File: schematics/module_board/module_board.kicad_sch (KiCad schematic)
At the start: 26 parts, among them J1 Conn_01x04_Male, J10 Conn_01x02_Male, J2 Conn_01x10_Male, J5 Conn_01x06_Male, J9 Conn_01x02_Male, U1 RP2040, U2 W25Q16JVSSIQ, Y1 ABLS-12.000MHZ-B4-T

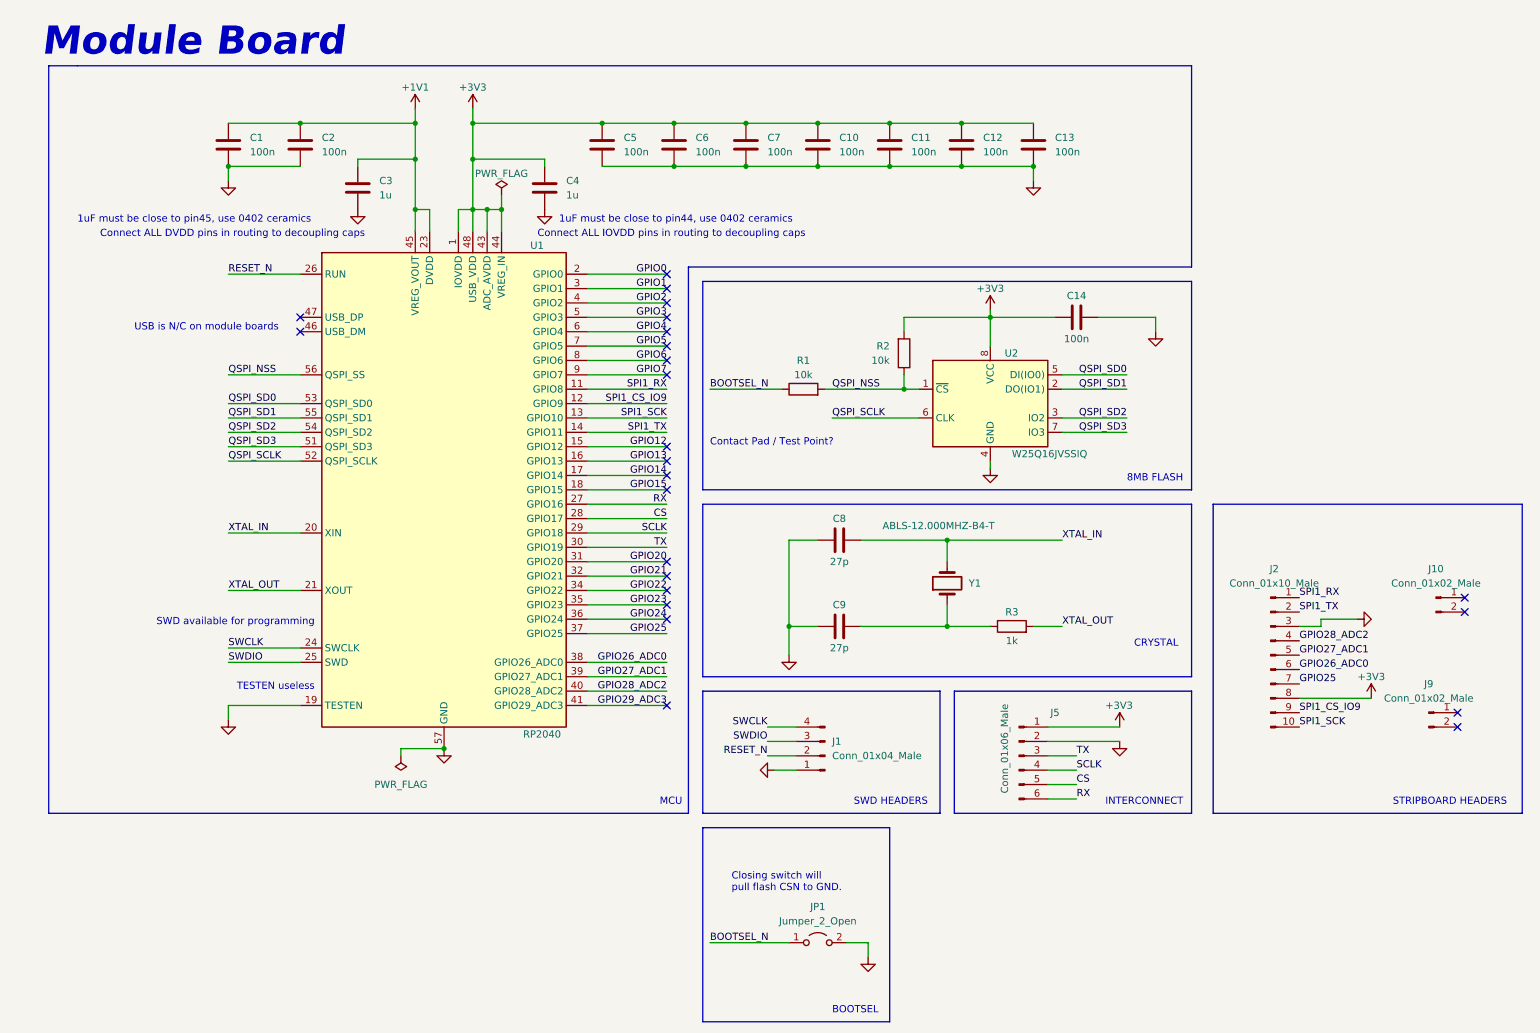
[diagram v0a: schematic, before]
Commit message: Added LED to Module Board
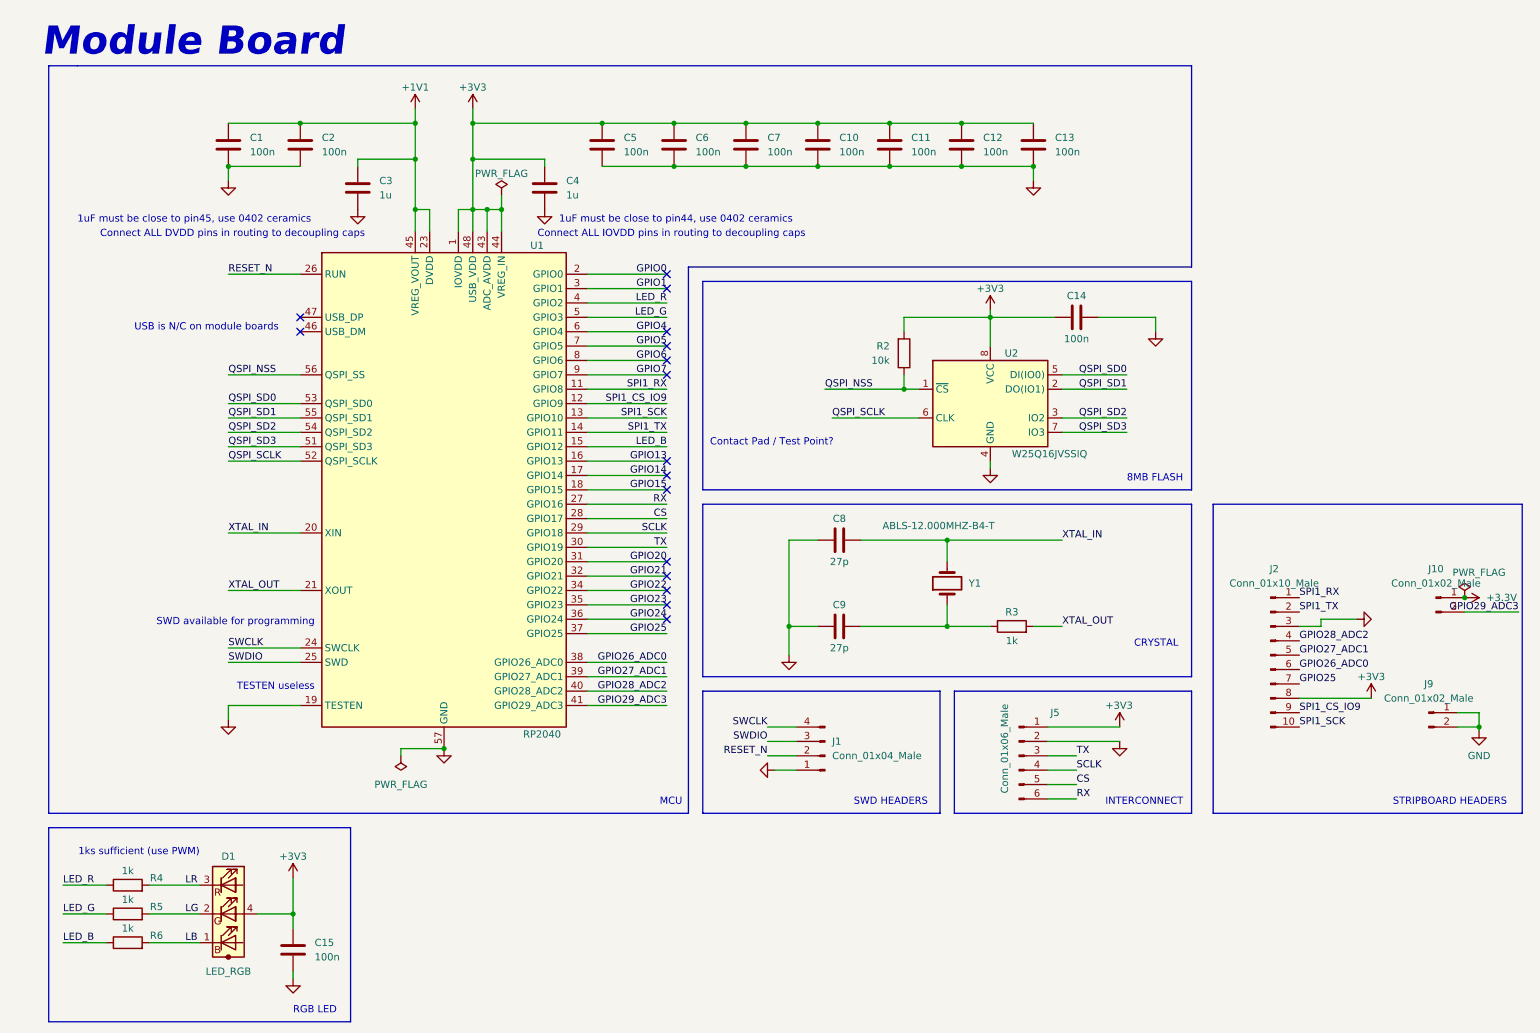
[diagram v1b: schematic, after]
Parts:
- removed JP1: Jumper_2_Open, Jumper:SolderJumper-2_P1.3mm_Open_Pad1.0x1.5mm, symbol Jumper:Jumper_2_Open
- removed R1: 10k, Resistor_SMD:R_0402_1005Metric, symbol Device:R
- added C15: 100n, Capacitor_SMD:C_0402_1005Metric, symbol Device:C
- added D1: LED_RGB, prototroller_footprints:LED_Cree-UHD111A, symbol prototroller_symbols:LED_RGB
- added R4, R5, R6: 1k, Resistor_SMD:R_0402_1005Metric, symbol Device:R
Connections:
- net +3V3: now also C15.1, D1.4 (A)
- net GND: now also J9.1 (Pin_1), J9.2 (Pin_2), C15.2
- net GPIO29_ADC3: now also J10.2 (Pin_2)
- net +3.3V: now reaches J10.1 (Pin_1)
- net GPIO12 renamed LED_B
- net LED_B: now also R6.1
- net GPIO2 renamed LED_R
- net LED_R: now also R4.1
- net GPIO3 renamed LED_G
- net LED_G: now also R5.1
- new net LB: D1.1 (B), R6.2
- new net LG: D1.2 (G), R5.2
- new net LR: D1.3 (R), R4.2
- no-connect marks 24 -> 16
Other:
- note added: "1ks sufficient (use PWM)"
- note added: "RGB LED"
- note removed: "BOOTSEL"
- note removed: "Closing switch will pull flash CSN to GND."

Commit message: master board rev b touchups
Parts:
- removed J1: Conn_01x04_Male, Connector_PinHeader_2.54mm:PinHeader_1x04_P2.54mm_Vertical, symbol Connector:Conn_01x04_Male
- added J1: Conn_01x03_Male, Connector_PinHeader_2.54mm:PinHeader_1x03_P2.54mm_Vertical, symbol Connector:Conn_01x03_Male
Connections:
- net +3.3V is gone; now on net +3V3: J10.1 (Pin_1)
- net RESET_N: now also J1.1 (Pin_1)
- net SWCLK: now also J1.3 (Pin_3)
- net SWDIO: now also J1.2 (Pin_2)
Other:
- note removed: "Contact Pad / Test Point?"
- moved on the sheet: C14, J10, R2, U2
